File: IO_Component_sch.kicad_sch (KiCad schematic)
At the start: 49 parts, among them SW10 SW_Push, SW11 SW_Push, SW12 SW_Push, SW13 SW_Push, SW14 SW_Push, SW15 SW_Push, SW16 SW_Push, SW17 SW_Push, SW18 SW_Push, SW19 SW_Push, SW20 SW_Push, SW21 SW_Push, SW22 SW_Push, SW23 SW_Push, SW24 SW_Push, SW25 SW_Push, SW26 SW_Push, SW27 SW_Push, SW28 SW_DIP_x08, SW3 SW_Push, SW4 SW_Push, SW5 SW_Push, SW6 SW_Push, SW7 SW_Push, SW8 SW_Push, SW9 SW_Push, U29 74LS30, U30 74LS138, U31 74LS04, U32 74LS244, U33 PAL16L8, U34 74LS374, U35 74LS374, U36 74LS374, U37 MAN71A, U38 MAN71A

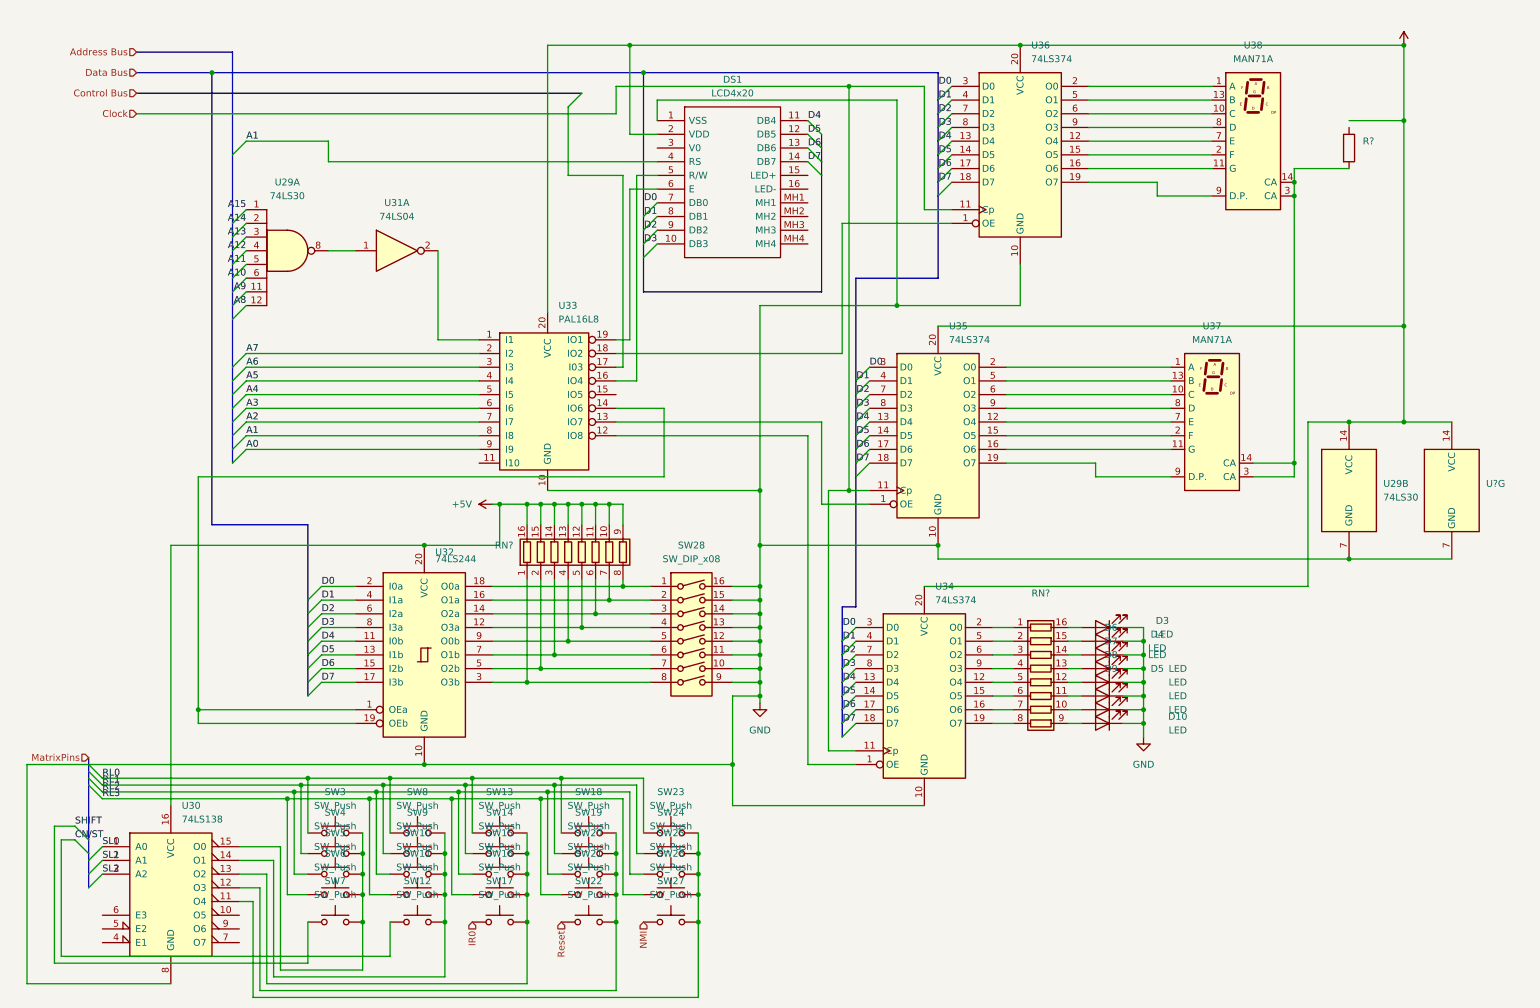
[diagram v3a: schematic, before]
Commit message: Enabled inputs on the max235
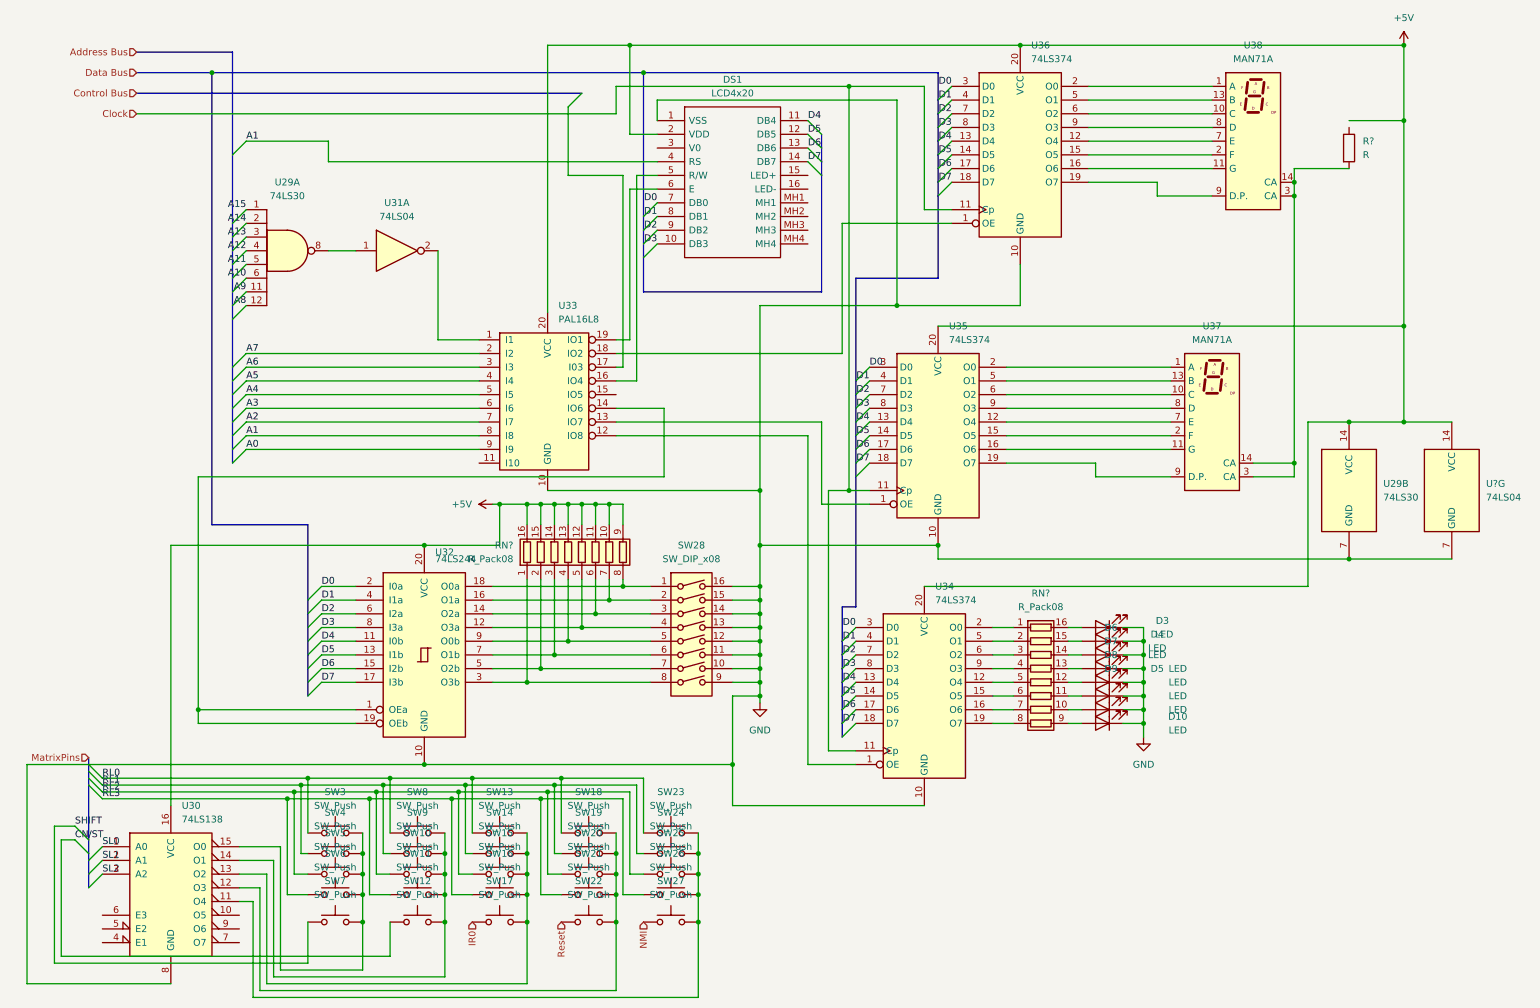
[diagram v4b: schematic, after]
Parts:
- R?: value (none) -> R
- RN? (x2): value (none) -> R_Pack08
- U?: value (none) -> 74LS04
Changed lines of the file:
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@@
     (in_bom yes) (on_board yes) (fields_autoplaced)
     (property "Reference" "RN?" (id 0) (at 201.93 121.92 90))
-    (property "Value" "" (id 1) (at 201.93 124.46 90))
+    (property "Value" "R_Pack08" (id 1) (at 201.93 124.46 90))
     (property "Footprint" "" (id 2) (at 201.93 150.495 90)
       (effects (font (size 1.27 1.27)) hide)
@@
       (effects (font (size 1.27 1.27)) (justify left))
     )
-    (property "Value" "" (id 1) (at 284.48 104.1399 0)
+    (property "Value" "74LS04" (id 1) (at 284.48 104.1399 0)
       (effects (font (size 1.27 1.27)) (justify left))
     )
@@
       (effects (font (size 1.27 1.27)) (justify right))
     )
-    (property "Value" "" (id 1) (at 104.14 115.5699 0)
+    (property "Value" "R_Pack08" (id 1) (at 104.14 115.5699 0)
       (effects (font (size 1.27 1.27)) (justify right))
     )
@@
       (effects (font (size 1.27 1.27)) hide)
     )
-    (property "Value" "" (id 1) (at 269.24 15.24 0))
+    (property "Value" "+5V" (id 1) (at 269.24 15.24 0))
     (property "Footprint" "" (id 2) (at 269.24 20.32 0)
       (effects (font (size 1.27 1.27)) hide)
@@
       (effects (font (size 1.27 1.27)) (justify left))
     )
-    (property "Value" "" (id 1) (at 261.62 40.6399 0)
-      (effects (font (size 1.27 1.27)) (justify left))
-    )
+    (property "Value" "R" (id 1) (at 261.62 40.6399 0)
+      (effects (font (size 1.27 1.27)) (justify left))
+    )

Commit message: Updated PCB
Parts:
- D10, D3, D4, D5, D6, D7, D8, D9: value LED -> (none); footprint LED_SMD:LED_0201_0603Metric -> (none)
- DS1: value LCD4x20 -> (none); footprint parts:LCD4x20 -> (none)
- R4: renamed from R?; value R -> (none)
- RN1, RN2: renamed from RN?; value R_Pack08 -> (none)
- SW10, SW11, SW12, SW13, SW14, SW15, SW16, SW17, SW18, SW19, SW20, SW21, SW22, SW23, SW24, SW25, SW26, SW27, SW3, SW4, SW5, SW6, SW7, SW8, SW9: value SW_Push -> (none); footprint Button_Switch_Keyboard:SW_Cherry_MX_1.00u_PCB -> (none)
- SW28: value SW_DIP_x08 -> (none); footprint Connector_DIN:DIN41612_D_2x8_Female_Vertical_THT -> (none)
- U29: value 74LS30 -> (none); footprint Package_DIP:PowerIntegrations_eDIP-12B -> (none)
- U30: value 74LS138 -> (none); footprint Package_DIP:DIP-16_W7.62mm -> (none)
- U31: value 74LS04 -> (none); footprint Package_DIP:DIP-14_W7.62mm -> (none)
- U32: value 74LS244 -> (none); footprint Package_DIP:DIP-20_W7.62mm -> (none)
- U33: value PAL16L8 -> (none); footprint Package_DIP:DIP-20_W7.62mm -> (none)
- U34, U35, U36: value 74LS374 -> (none); footprint Package_DIP:DIP-20_W7.62mm -> (none)
- U37, U38: value MAN71A -> (none); footprint Display_7Segment:MAN71A -> (none)
- U41: renamed from U?; value 74LS04 -> (none)

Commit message: PCB wiring
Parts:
- D10, D3, D4, D5, D6, D7, D8, D9: value (none) -> LED; footprint (none) -> LED_SMD:LED_0201_0603Metric
- DS1: value (none) -> LCD4x20; footprint (none) -> parts:LCD4x20
- R4: value (none) -> R
- RN1, RN2: value (none) -> R_Pack08
- SW10, SW11, SW12, SW13, SW14, SW15, SW16, SW17, SW18, SW19, SW20, SW21, SW22, SW23, SW24, SW25, SW26, SW27, SW3, SW4, SW5, SW6, SW7, SW8, SW9: value (none) -> SW_Push; footprint (none) -> Button_Switch_Keyboard:SW_Cherry_MX_1.00u_PCB
- SW28: value (none) -> SW_DIP_x08; footprint (none) -> Connector_DIN:DIN41612_D_2x8_Female_Vertical_THT
- U29: value (none) -> 74LS30; footprint (none) -> Package_DIP:PowerIntegrations_eDIP-12B
- U30: value (none) -> 74LS138; footprint (none) -> Package_DIP:DIP-16_W7.62mm
- U31, U41: value (none) -> 74LS04; footprint (none) -> Package_DIP:DIP-14_W7.62mm
- U32: value (none) -> 74LS244; footprint (none) -> Package_DIP:DIP-20_W7.62mm
- U33: value (none) -> PAL16L8; footprint (none) -> Package_DIP:DIP-20_W7.62mm
- U34, U35, U36: value (none) -> 74LS374; footprint (none) -> Package_DIP:DIP-20_W7.62mm
- U37, U38: value (none) -> MAN71A; footprint (none) -> Display_7Segment:MAN71A
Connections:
- net +5V: now also R4.1

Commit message: More PCB wiring
Wired all components to eachother, did not interface everything with the 8086
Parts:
- RN1, RN2: footprint (none) -> Package_DIP:DIP-16_W7.62mm
- SW28: footprint Connector_DIN:DIN41612_D_2x8_Female_Vertical_THT -> (none)
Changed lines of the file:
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@@
     (property "Reference" "RN2" (id 0) (at 201.93 121.92 90))
     (property "Value" "R_Pack08" (id 1) (at 201.93 124.46 90))
-    (property "Footprint" "" (id 2) (at 201.93 150.495 90)
+    (property "Footprint" "Package_DIP:DIP-16_W7.62mm" (id 2) (at 201.93 150.495 90)
       (effects (font (size 1.27 1.27)) hide)
     )
@@
       (effects (font (size 1.27 1.27)) (justify right))
     )
-    (property "Footprint" "" (id 2) (at 128.905 114.3 90)
+    (property "Footprint" "Package_DIP:DIP-16_W7.62mm" (id 2) (at 128.905 114.3 90)
       (effects (font (size 1.27 1.27)) hide)
     )
@@
     (property "Reference" "SW28" (id 0) (at 137.16 113.03 0))
     (property "Value" "SW_DIP_x08" (id 1) (at 137.16 115.57 0))
-    (property "Footprint" "Connector_DIN:DIN41612_D_2x8_Female_Vertical_THT" (id 2) (at 137.16 130.81 0)
-      (effects (font (size 1.27 1.27)) hide)
-    )
+    (property "Footprint" "" (id 2) (at 137.16 130.81 0)
+      (effects (font (size 1.27 1.27)) hide)
+    )

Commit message: Fixed Incorrect Data Pin labels in memory
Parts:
- R4: footprint (none) -> Resistor_SMD:R_0201_0603Metric
- SW28: footprint (none) -> Button_Switch_SMD:SW_DIP_SPSTx08_Slide_6.7x21.88mm_W6.73mm_P2.54mm_LowProfile_JPin
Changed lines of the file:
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@@
       (effects (font (size 1.27 1.27)) (justify left))
     )
-    (property "Footprint" "" (id 2) (at 257.302 39.37 90)
+    (property "Footprint" "Resistor_SMD:R_0201_0603Metric" (id 2) (at 257.302 39.37 90)
       (effects (font (size 1.27 1.27)) hide)
     )
@@
     (property "Reference" "SW28" (id 0) (at 137.16 113.03 0))
     (property "Value" "SW_DIP_x08" (id 1) (at 137.16 115.57 0))
-    (property "Footprint" "" (id 2) (at 137.16 130.81 0)
-      (effects (font (size 1.27 1.27)) hide)
-    )
+    (property "Footprint" "Button_Switch_SMD:SW_DIP_SPSTx08_Slide_6.7x21.88mm_W6.73mm_P2.54mm_LowProfile_JPin" (id 2) (at 137.16 130.81 0)
+      (effects (font (size 1.27 1.27)) hide)
+    )
